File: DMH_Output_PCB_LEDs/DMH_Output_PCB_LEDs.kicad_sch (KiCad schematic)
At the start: 14 parts, among them J1 TS_Jack_6.35mm_Sw, J2 TS_Jack_6.35mm_Sw, J200 IDC_02x05, J21 Conn_01x02, J22 Conn_01x02, J24 Conn_01x02, J25 Conn_01x02, J3 TRS Jack 6.35mm, J4 TRS Jack 6.35mm, J5 TRS Jack 6.35mm, J6 TS_Jack_6.35mm_Sw, J7 TS_Jack_6.35mm_Sw, J8 TS_Jack_6.35mm_Sw, J9 TS_Jack_6.35mm_Sw

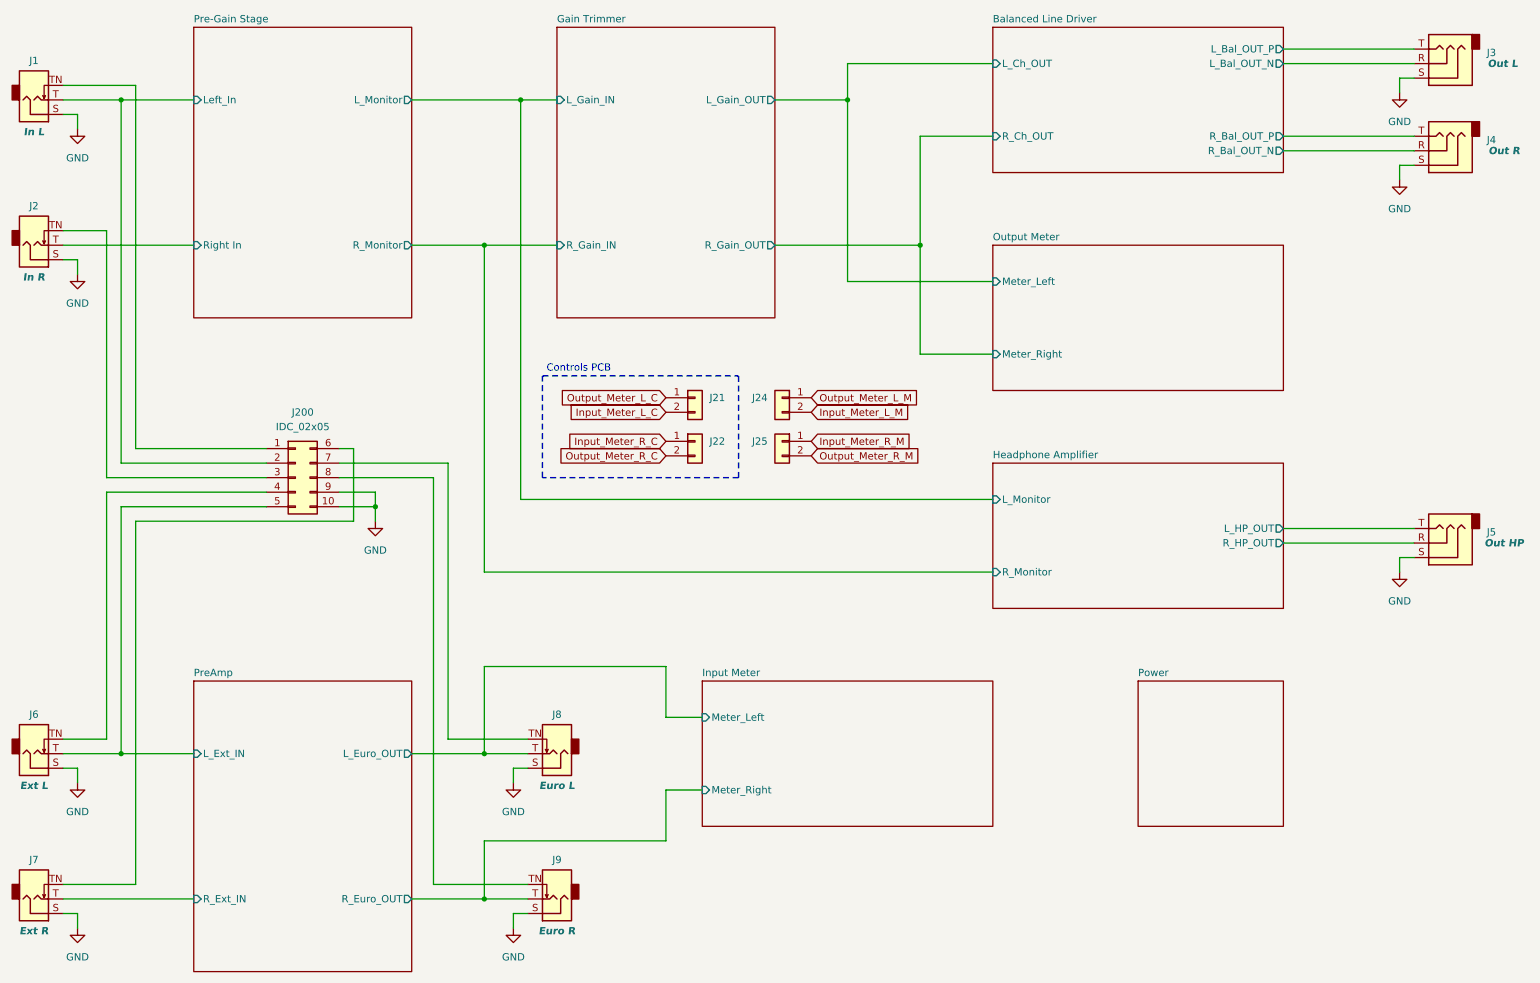
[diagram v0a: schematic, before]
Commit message: Adjusted output meter resistors
... and deleted unnecessary notes
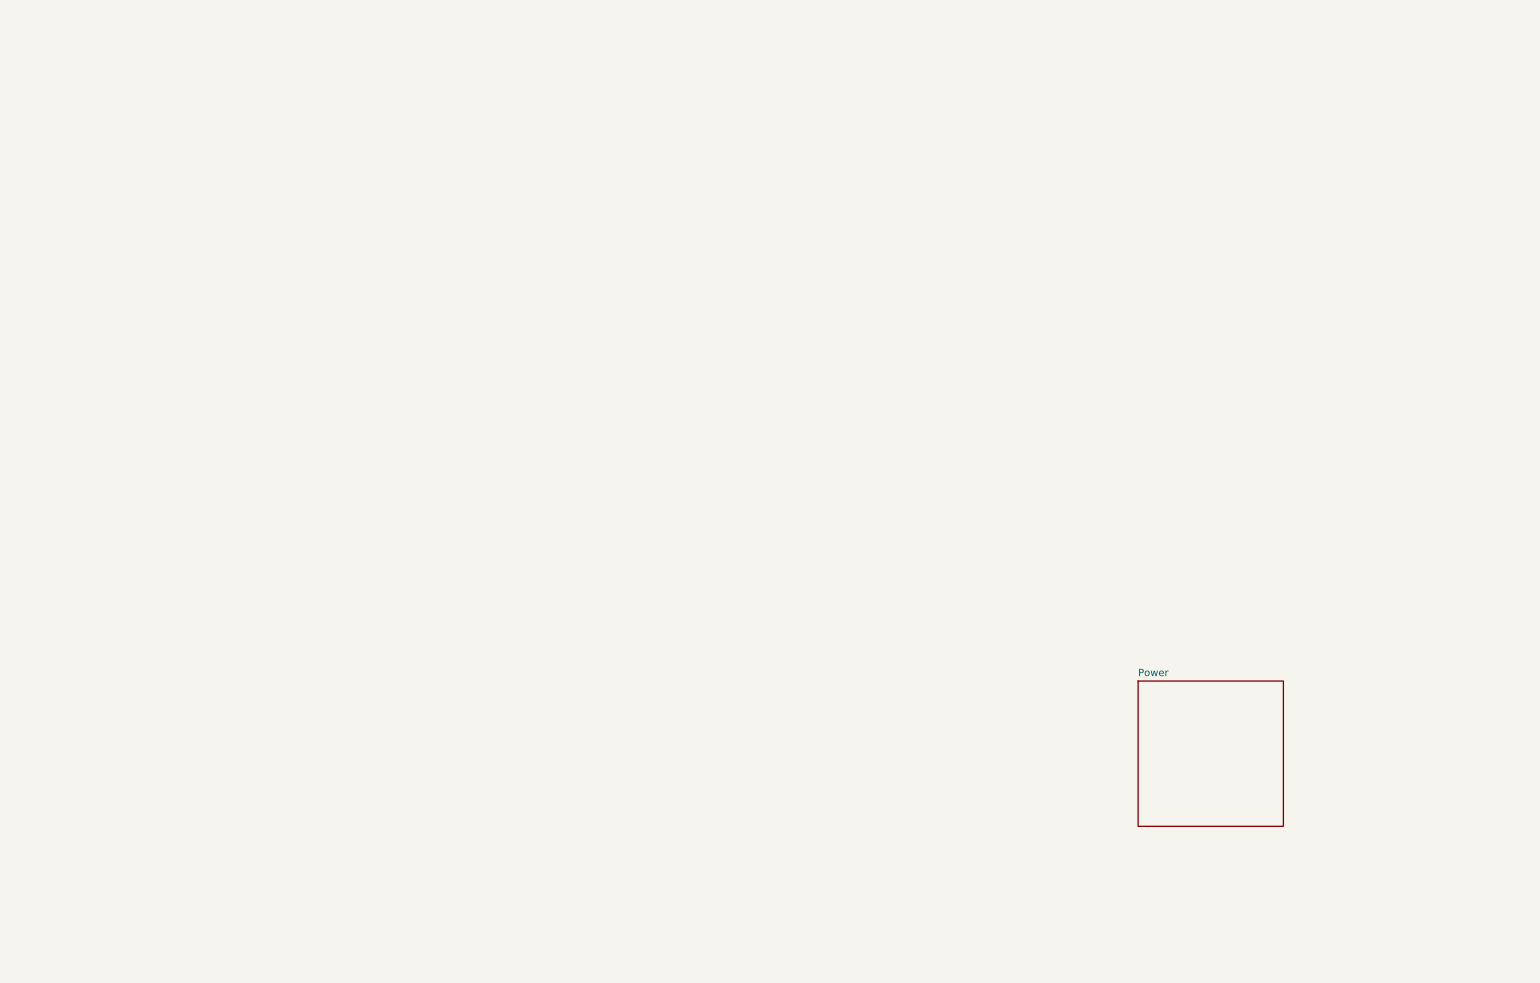
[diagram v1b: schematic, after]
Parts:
- removed J1, J2, J6, J7, J8, J9: TS_Jack_6.35mm_Sw, SynthStuff:CUI_MJ-63052A, symbol SynthStuff:TS_Jack_6.35mm_Sw
- removed J200: IDC_02x05, SynthStuff:IDC-Header_2x05_P2.54mm_Vertical_BackBone, symbol SynthStuff:BackBone_Connector_10Pin
- removed J21, J22: Conn_01x02, Connector_PinSocket_2.54mm:PinSocket_1x02_P2.54mm_Vertical, symbol Connector_Generic:Conn_01x02
- removed J24, J25: Conn_01x02, Connector_PinHeader_2.54mm:PinHeader_1x02_P2.54mm_Vertical, symbol Connector_Generic:Conn_01x02
- removed J3, J4, J5: TRS Jack 6.35mm, SynthStuff:CUI_SJ-63083A, symbol Connector_Audio:AudioJack3
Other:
- removed sheet Balanced Line Driver
- removed sheet Gain Trimmer
- removed sheet Headphone Amplifier
- removed sheet Input Meter
- removed sheet Output Meter
- removed sheet Pre-Gain Stage
- removed sheet PreAmp
- note removed: "Controls PCB"
